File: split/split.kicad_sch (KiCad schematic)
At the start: 49 parts, among them SW1 SW_Push_45deg, SW10 SW_Push_45deg, SW11 SW_Push_45deg, SW12 SW_Push_45deg, SW13 SW_Push_45deg, SW14 SW_Push_45deg, SW15 SW_Push_45deg, SW16 SW_Push_45deg, SW17 SW_Push_45deg, SW18 SW_Push_45deg, SW19 SW_Push_45deg, SW2 SW_Push_45deg, SW20 SW_Push_45deg, SW21 SW_Push_45deg, SW22 SW_Push_45deg, SW23 SW_Push_45deg, SW24 SW_Push_45deg, SW3 SW_Push_45deg, SW4 SW_Push_45deg, SW5 SW_Push_45deg, SW6 SW_Push_45deg, SW7 SW_Push_45deg, SW8 SW_Push_45deg, SW9 SW_Push_45deg, U1 Arduino_Pro_Micro

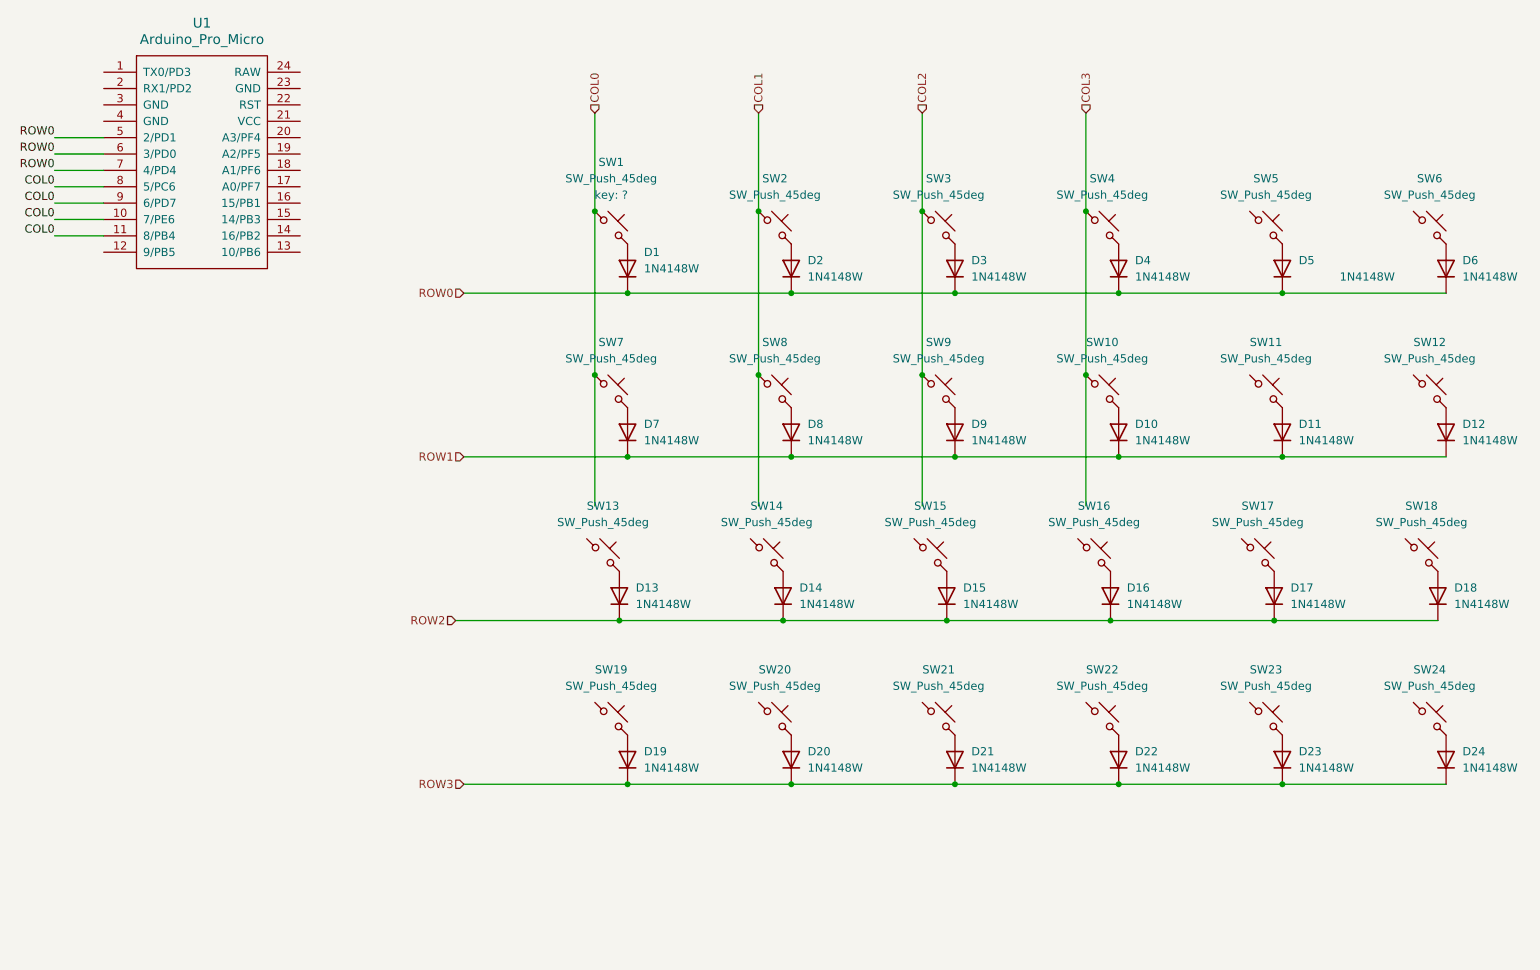
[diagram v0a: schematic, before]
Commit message: start split rigth layout
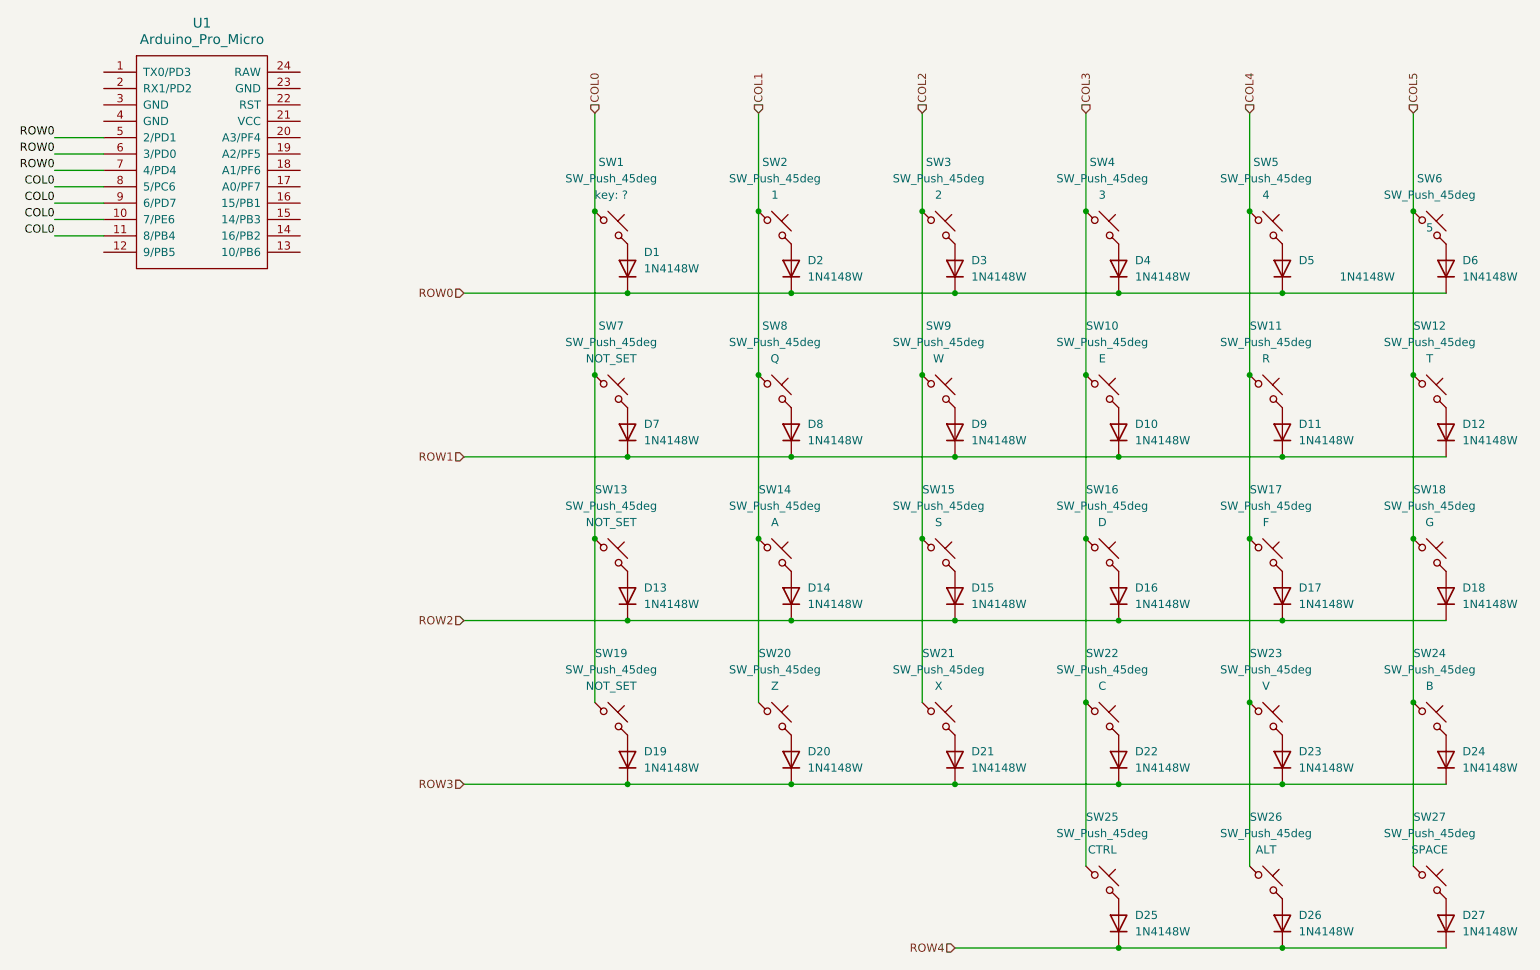
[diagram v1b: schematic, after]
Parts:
- added D25, D26, D27: 1N4148W, Diode_SMD:D_SOD-123, symbol Device:D
- added SW25, SW26, SW27: SW_Push_45deg, ScottoKeebs_MX:MX_PCB_1.00u, symbol Switch:SW_Push_45deg
- SW10: key not_set -> E
- SW11: key not_set -> R
- SW12: key not_set -> T
- SW13, SW19: key not_set -> NOT_SET
- SW14: key not_set -> A
- SW15: key not_set -> S
- SW16: key not_set -> D
- SW17: key not_set -> F
- SW18: key not_set -> G
- SW2: key Q -> 1
- SW20: key not_set -> Z
- SW21: key not_set -> X
- SW22: key not_set -> C
- SW23: key not_set -> V
- SW24: key not_set -> B
- SW3: key W -> 2
- SW4: key E -> 3
- SW5: key R -> 4
- SW6: key T -> 5
- SW7: key ? -> NOT_SET
- SW8: key A -> Q
- SW9: key S -> W
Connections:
- net COL0: now also SW13.1, SW19.1
- net COL1: now also SW14.1, SW20.1
- net COL2: now also SW15.1, SW21.1
- net COL3: now also SW16.1, SW22.1, SW25.1
- net COL4: now reaches SW17.1
- net COL4: now also SW11.1, SW23.1, SW5.1, SW26.1
- net COL5: now reaches SW12.1
- net COL5: now also SW18.1, SW24.1, SW6.1, SW27.1
- new net: D25.2 (A), SW25.2
- new net: D27.2 (A), SW27.2
- new net: D26.2 (A), SW26.2
- new net ROW4: D25.1 (K), D26.1 (K), D27.1 (K)
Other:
- moved on the sheet: D13, D14, D15, D16, D17, D18, SW13, SW14, SW15, SW16, SW17, SW18

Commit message: add arduino pro micro equivalent MCU schematic
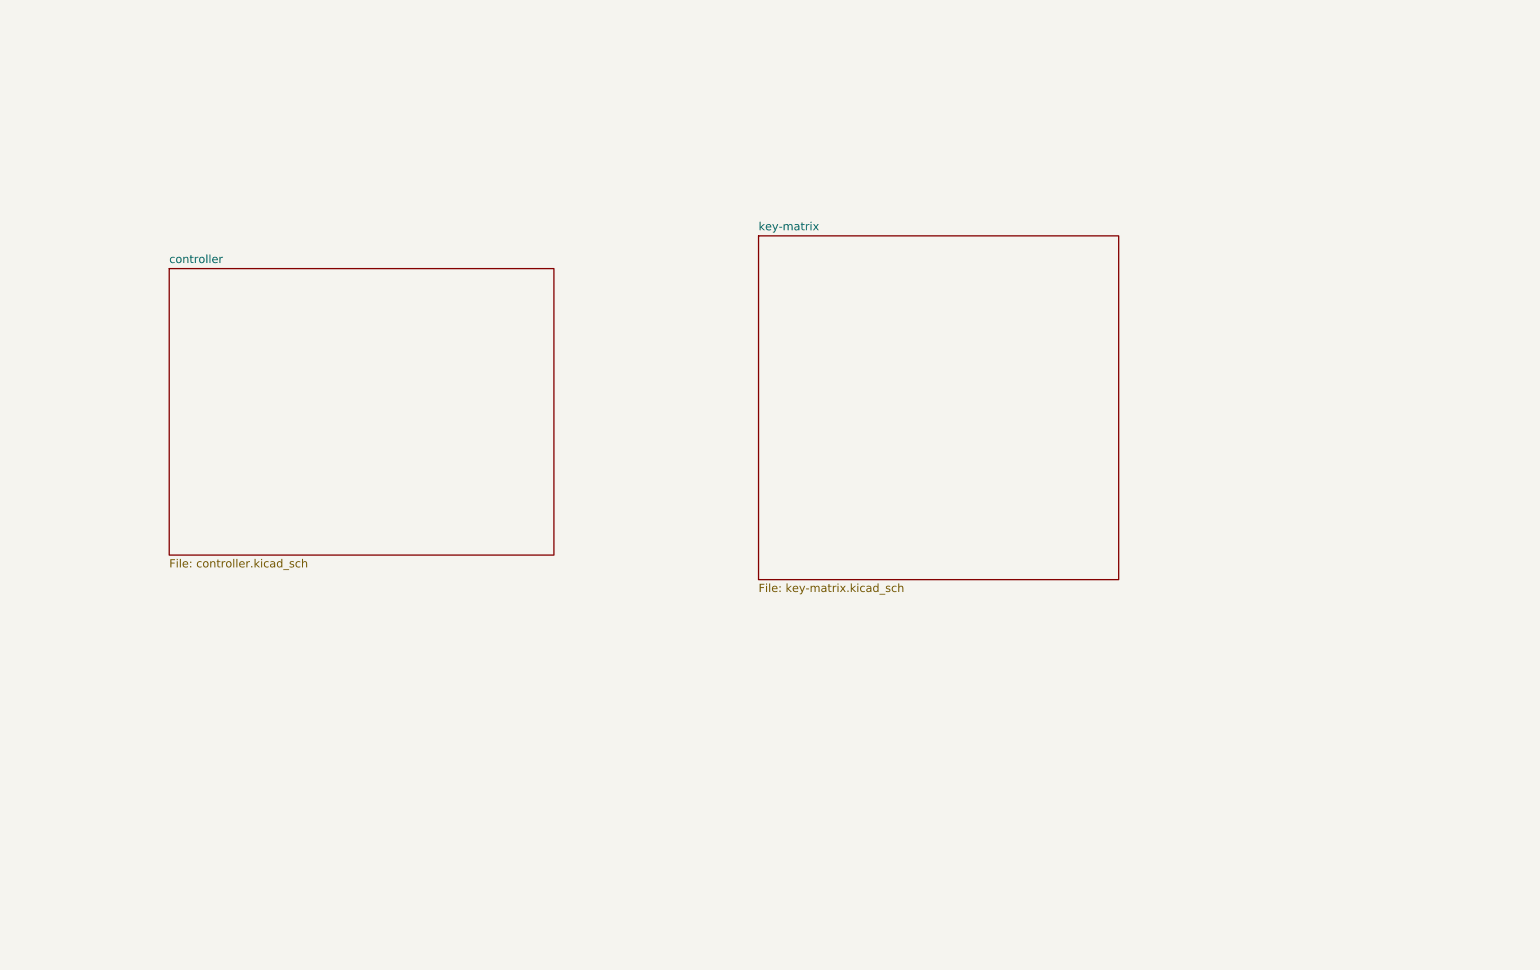
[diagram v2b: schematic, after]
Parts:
- removed D1, D10, D11, D12, D13, D14, D15, D16, D17, D18, D19, D2, D20, D21, D22, D23, D24, D25, D26, D27, D3, D4, D5, D6, D7, D8, D9: 1N4148W, Diode_SMD:D_SOD-123, symbol Device:D
- removed SW1, SW10, SW11, SW12, SW13, SW14, SW15, SW16, SW17, SW18, SW19, SW2, SW20, SW21, SW22, SW23, SW24, SW25, SW26, SW27, SW3, SW4, SW5, SW6, SW7, SW8, SW9: SW_Push_45deg, ScottoKeebs_MX:MX_PCB_1.00u, symbol Switch:SW_Push_45deg
- removed U1: Arduino_Pro_Micro, ScottoKeebs_MCU:Arduino_Pro_Micro, symbol ScottoKicad:MCU_Arduino_Pro_Micro
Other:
- added sheet controller (controller.kicad_sch)
- added sheet key-matrix (key-matrix.kicad_sch)
